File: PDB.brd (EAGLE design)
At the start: 130.3 x 166.9 mm, 53 parts, among them J1 B06B-HCMKK, J2 B06B-HCMKK, J3 SS-6488-NF-A431, J4 SS-6488-NF-A431, J5 B06B-HCMKK, J6 B03B-HCMKS, J7 B03B-HCMKS, J8 SS-6488-NF-A431

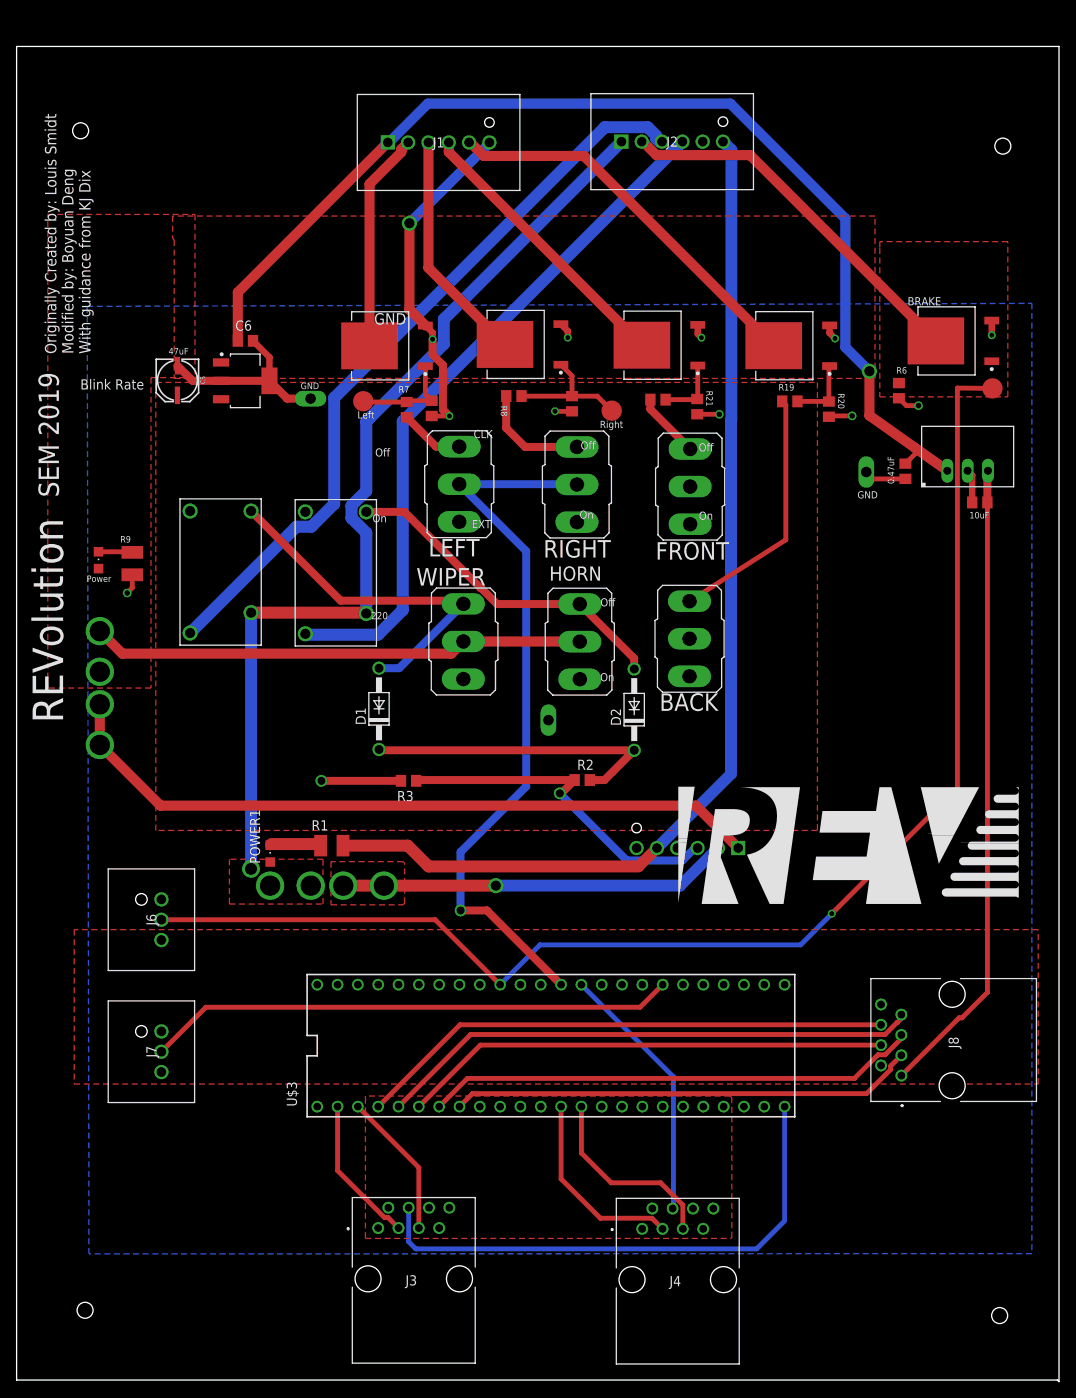
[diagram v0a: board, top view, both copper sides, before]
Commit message: Flipped all connectors to the back side, added capacitors connecting Teensy's 5V_REG to GND
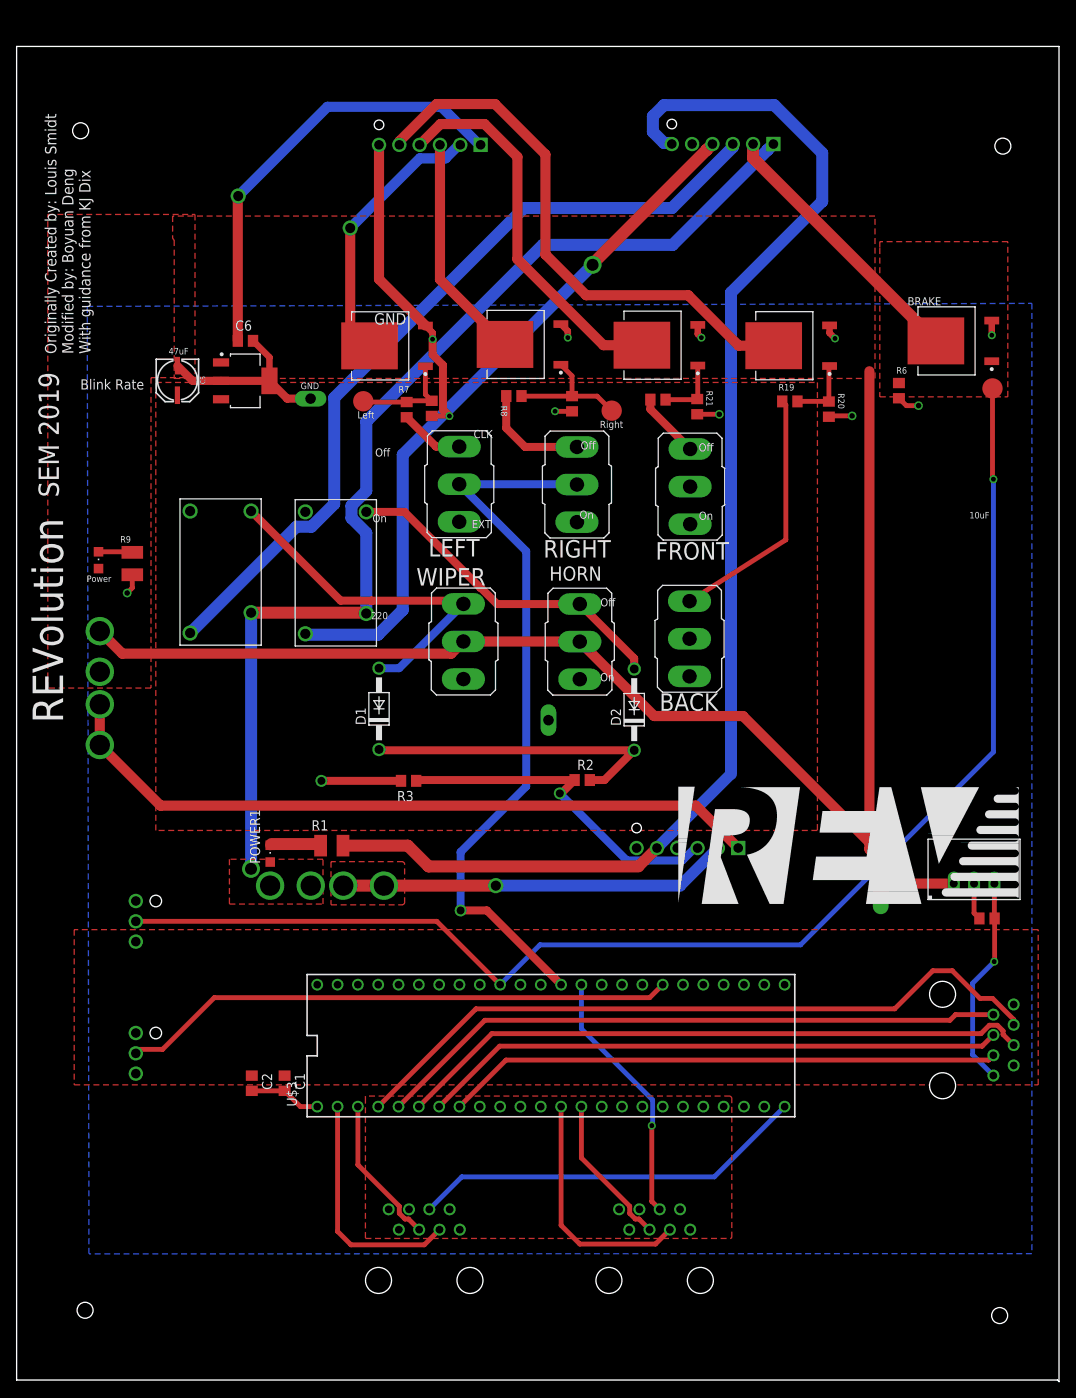
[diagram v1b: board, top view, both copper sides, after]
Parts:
- added C1: 0.1uF, rcl:C0805
- added C2: 10uF, rcl:C0805
- moved TP12 53.3 mm to (109.9, 48.1)
- moved C8 52.5 mm to (112.8, 49.0)
- moved C7 52.0 mm to (123.2, 45.6)
- moved TRACO 51.6 mm to (121.6, 50.0)
- moved J2 19.0 mm to (96.5, 142.4), flipped to the bottom
- moved J1 11.6 mm to (59.9, 142.3), flipped to the bottom
- moved J8 11.5 mm to (124.0, 26.0), flipped to the bottom
- moved J3 10.2 mm to (57.3, 6.70), flipped to the bottom
- moved J4 6.00 mm to (86.1, 6.70), flipped to the bottom
- moved J7 3.21 mm to (16.8, 26.2), flipped to the bottom
- moved J6 3.21 mm to (16.8, 42.7), flipped to the bottom
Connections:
- net 5V_REG: now also C1.1, C2.1
- net GND: now also C1.2, C2.2
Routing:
- net 5V_REG: track 80.3 -> 26.2 mm, vias 0 -> 1
- net VDD: track 199.8 -> 235.5 mm
- net IGND: track 133.9 -> 165.9 mm
- net CLK_SW: track 67.1 -> 89.7 mm
- net REARLIGHT_SIG: track 48.6 -> 69.0 mm
- net CS: track 61.0 -> 79.9 mm
- net CLK_A: track 67.3 -> 49.7 mm
- net IVDD: track 120.2 -> 137.3 mm
- net BRAKE_SIG: track 47.1 -> 34.1 mm
- net HEADLIGHT_SIG: track 35.3 -> 47.8 mm
- net RESET: track 58.2 -> 69.4 mm
- net DC: track 61.7 -> 73.0 mm
- net MOSI_A: track 18.6 -> 29.8 mm
- net MOSI_SW: track 67.9 -> 79.1 mm
- net WIPER: track 93.9 -> 101.2 mm
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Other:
- board text removed: "0.47uF"

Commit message: Silkscreen finished.
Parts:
- moved TP11 15.0 mm to (82.8, 66.1)
- moved C2 5.02 mm to (31.8, 30.0)
- moved C1 5.02 mm to (35.8, 30.0)
- moved BACK 0.50 mm to (85.7, 80.2)
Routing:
- net 5V_REG: track 26.2 -> 38.1 mm
- net GND: track 108.3 -> 114.7 mm
- net HORN: track 87.8 -> 88.9 mm
- net H7: track 31.8 -> 32.3 mm
- net PEDAL_SNS: vias 0 -> 1
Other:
- board text added: "BRAKE_SIG"
- board text added: "Brake"
- board text added: "Breakout1"
- board text added: "Breakout2"
- board text added: "Fuse Aux"
- board text added: "Fuse Independent"
- board text added: "HAZ_L_SIG"
- board text added: "HAZ_R_SIG"
- board text added: "HEAD_LIGHT"
- board text added: "HORN"
- board text added: "HORN RELAY"
- board text added: "Head"
- board text added: "IGND"
- board text added: "ISOENABLE"
- board text added: "IVDD"
- board text added: "Input"
- board text added: "MCU1"
- board text added: "MCU2"
- board text added: "Noise Prevention"
- board text added: "Pedal"
- board text added: "REAR_LIGHT"
- board text added: "Rear"
- board text added: "Screen"
- board text added: "TI Voltage Regulator"
- board text added: "TRACO"
- board text added: "VDD"
- board text added: "WIPER"
- board text added: "WIPER RELAY"
- board text removed: "Blink Rate"
- board text removed: "CLK"
- board text removed: "EXT"

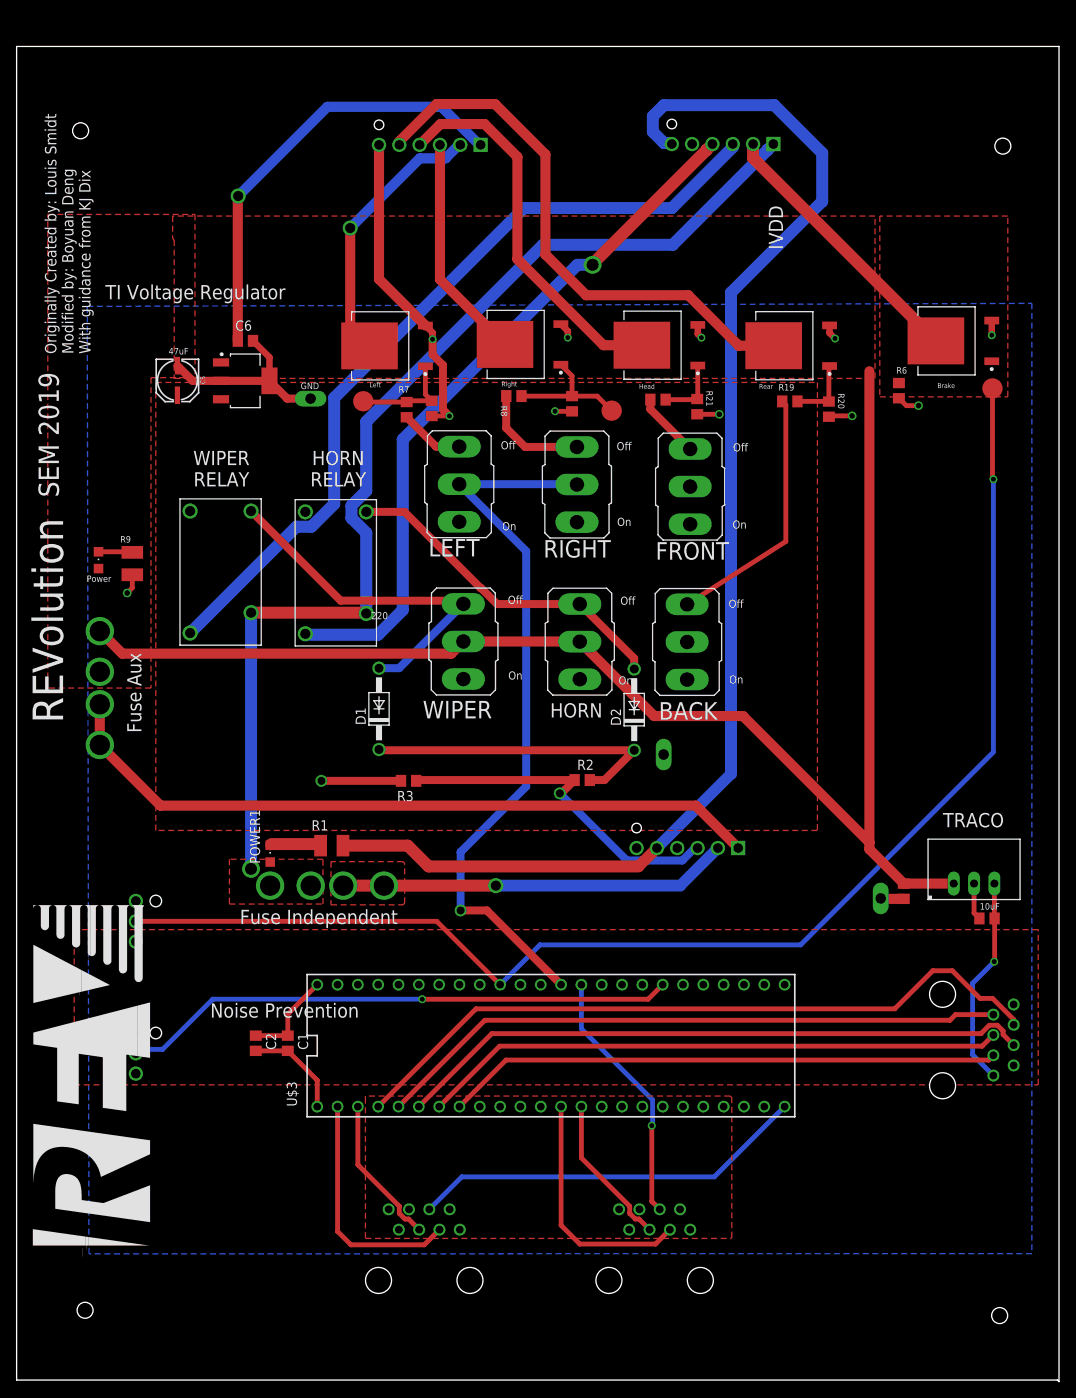
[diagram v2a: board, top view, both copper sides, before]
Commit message: slightly moved traces that were close
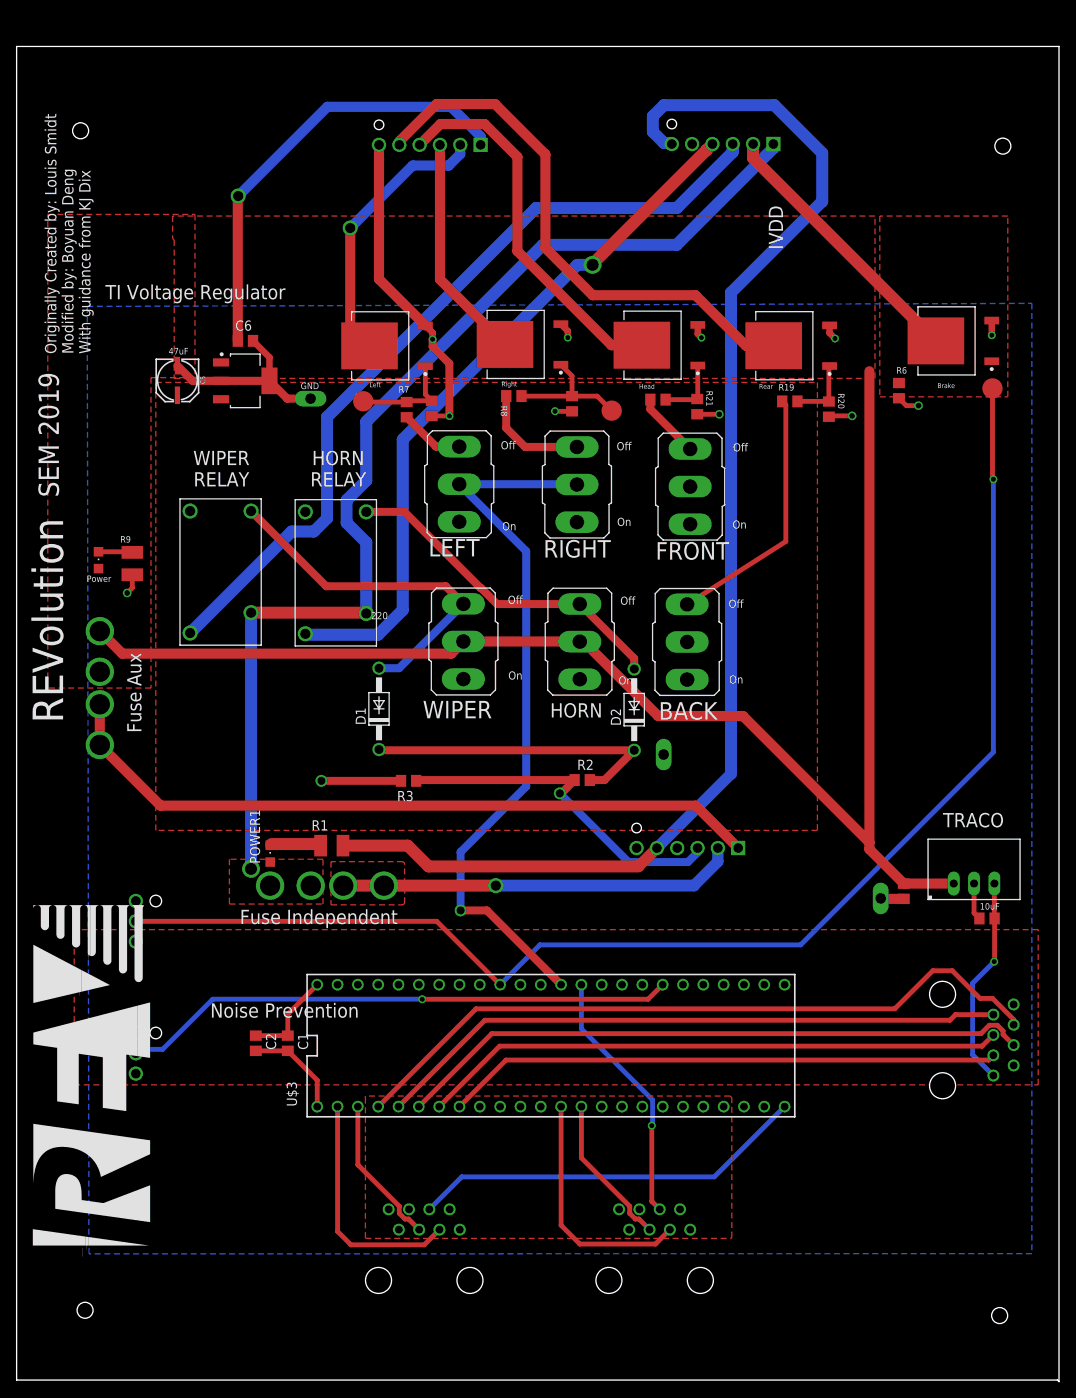
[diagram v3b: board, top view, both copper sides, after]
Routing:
- net N$8: track 48.8 -> 49.8 mm
- net IVDD: track 137.3 -> 138.1 mm
- net HAZ_L_SIG: track 33.8 -> 34.5 mm
- net VDD: track 235.5 -> 236.1 mm
- net HEADLIGHT_SIG: track 47.8 -> 47.2 mm
